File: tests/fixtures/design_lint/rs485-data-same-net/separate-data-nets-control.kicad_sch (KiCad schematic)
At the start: 1 part, among them U1 RS-485 transceiver

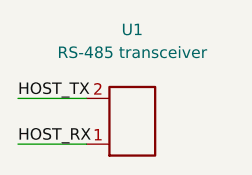
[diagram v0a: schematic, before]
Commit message: fix(lint): correct RS-485 native control labels
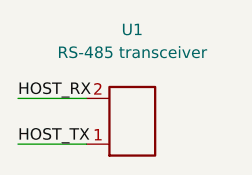
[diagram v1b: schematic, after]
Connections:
- net HOST_RX: now also U1.2 (R); no longer U1.1 (D)
- net HOST_TX: now also U1.1 (D); no longer U1.2 (R)
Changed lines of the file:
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@@
   (wire (pts (xy 58.42 60.96) (xy 50.80 60.96))
     (stroke (width 0) (type default)))
-  (label "HOST_TX" (at 50.80 60.96 0)
+  (label "HOST_RX" (at 50.80 60.96 0)
     (effects (font (size 1.27 1.27)) (justify left bottom))
 )
   (wire (pts (xy 58.42 66.04) (xy 50.80 66.04))
     (stroke (width 0) (type default)))
-  (label "HOST_RX" (at 50.80 66.04 0)
+  (label "HOST_TX" (at 50.80 66.04 0)
     (effects (font (size 1.27 1.27)) (justify left bottom))
 )
